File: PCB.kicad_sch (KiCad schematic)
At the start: 20 parts, among them SW1 SW_Push_Dual, SW10 SW_Push_Dual, SW11 SW_Push_Dual, SW12 SW_Push_Dual, SW13 SW_Push_Dual, SW2 SW_Push_Dual, SW5 SW_Push_Dual, SW6 SW_Push_Dual, SW7 SW_Push_Dual, SW8 SW_Push_Dual, SW9 SW_Push_Dual, U1 STM32L010F4Px, U2 74HC165, U3 74HC165, U4 74HC165

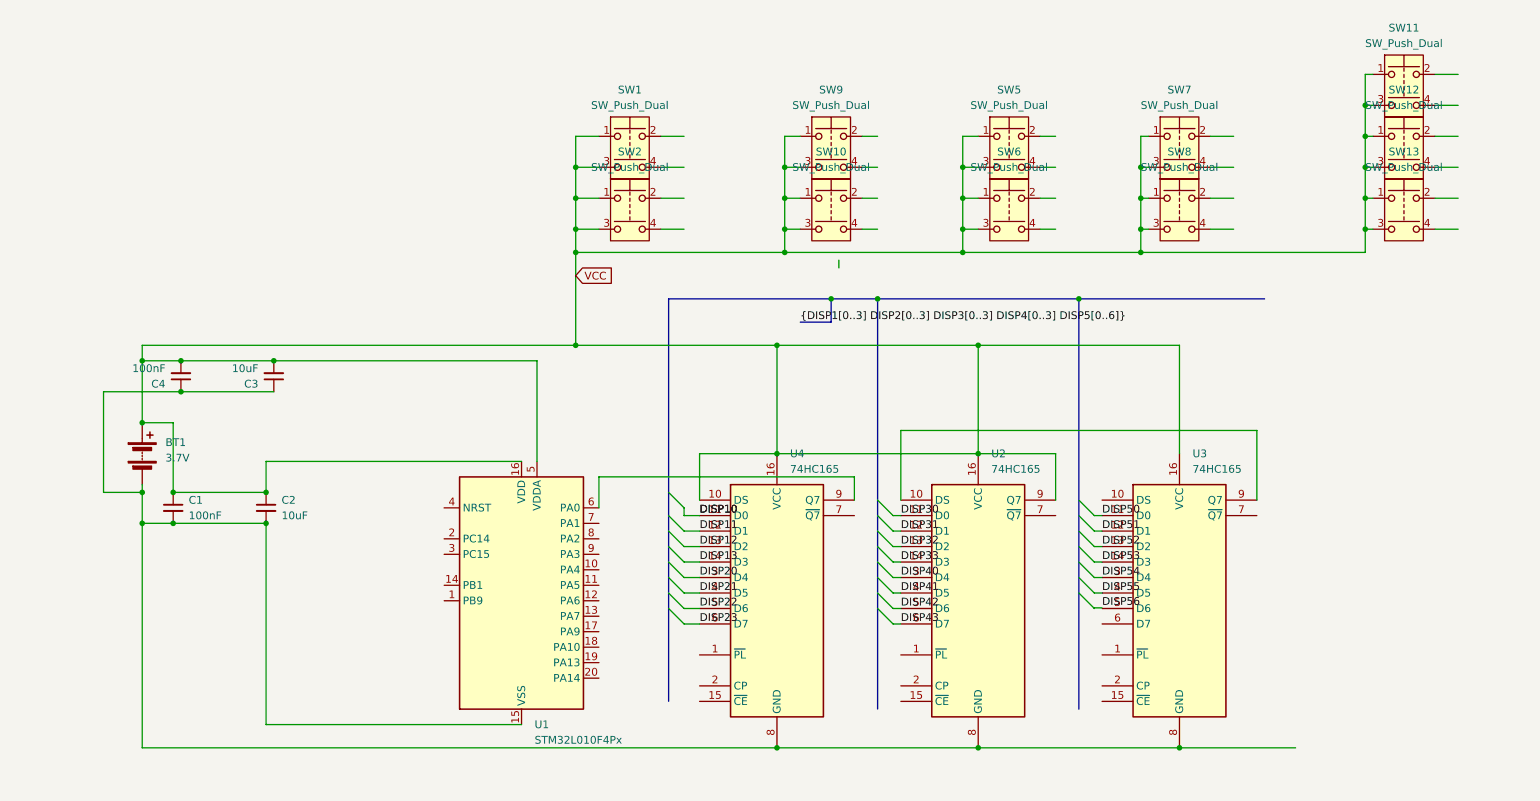
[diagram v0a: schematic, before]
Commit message: botones
añadidas las conexiones de los botones con pull down resistors
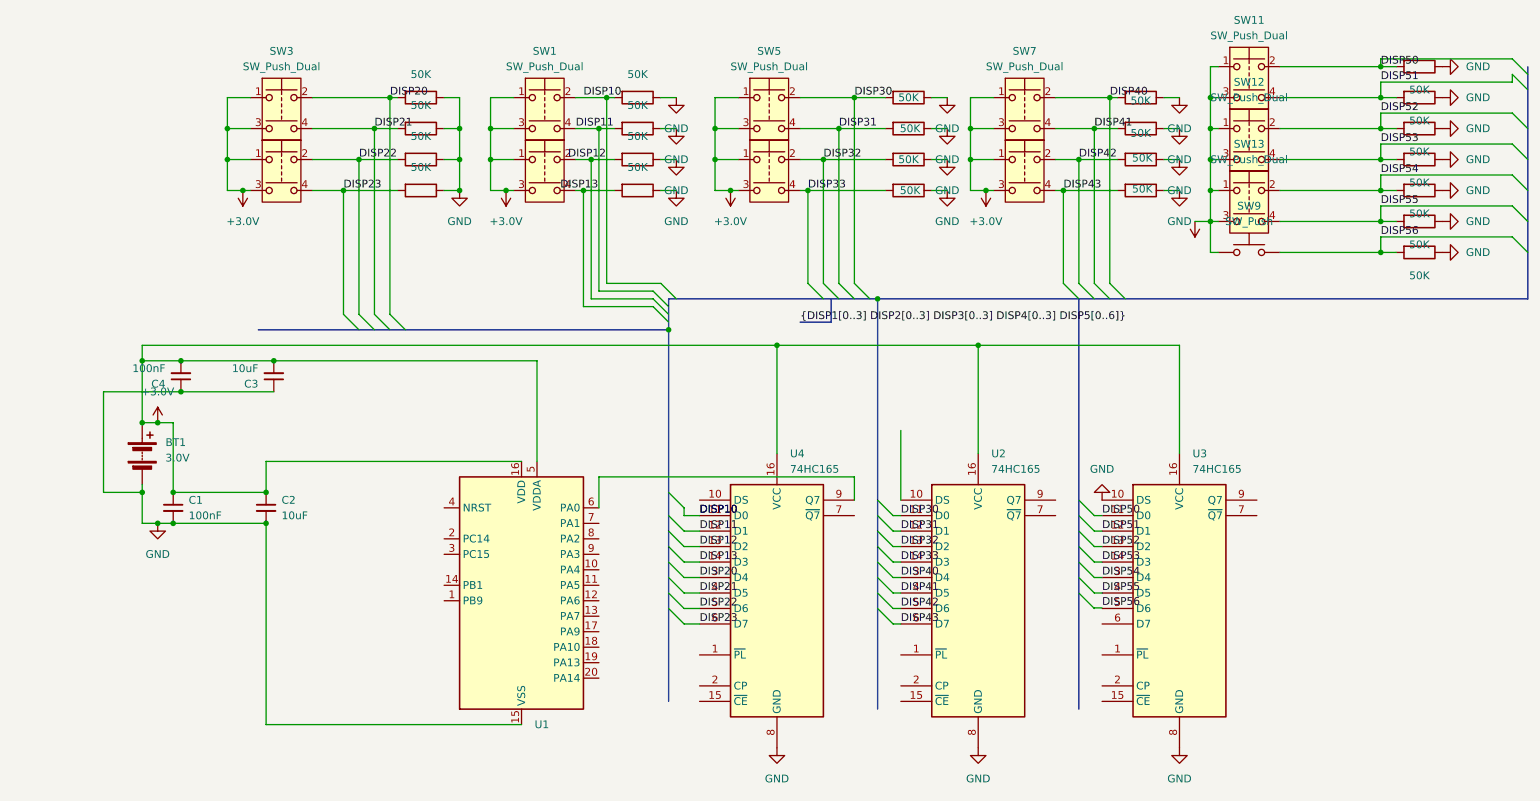
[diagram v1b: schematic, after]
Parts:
- removed SW10, SW9: SW_Push_Dual, symbol Switch:SW_Push_Dual
- added R, R1, R10, R11, R12, R13, R14, R15, R16, R2, R23, R24, R25, R26, R27, R28, R29, R3, R4, R5, R6, R7, R9: 50K, symbol Device:R
- added SW3, SW4: SW_Push_Dual, symbol Switch:SW_Push_Dual
- added SW9: SW_Push, symbol Switch:SW_Push
- BT1: value 3.7V -> 3.0V
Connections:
- net DISP10: now also SW1.2, R1.2
- net DISP11: now also SW1.4, R2.2
- net DISP20: now also R5.2, SW3.2
- net DISP21: now also R6.2, SW3.4
- net DISP22: now also R7.2, SW4.2
- net DISP23: now also R.2, SW4.4
- net DISP30: now also SW5.2, R9.2
- net DISP31: now also SW5.4, R10.2
- net DISP32: now also SW6.2, R11.2
- net DISP33: now also SW6.4, R12.2
- net DISP40: now also SW7.2, R13.2
- net DISP41: now also SW7.4, R14.2
- net DISP42: now also SW8.2, R15.2
- net DISP43: now also SW8.4, R16.2
- net DISP50: now also SW11.2, R29.2
- net DISP51: now also SW11.4, R28.2
- net DISP52: now also SW12.2, R27.2
- net DISP53: now also SW12.4, R26.2
- net DISP54: now also SW13.2, R25.2
- net DISP55: now also SW13.4, R24.2
- net DISP56: now also R23.2, SW9.2
- net GND: now reaches BT1.2 (-), C1.2, C2.2, C3.1, C4.1, U1.15 (VSS), U2.8 (GND), U3.8 (GND), U4.8 (GND)
- net GND: now also U3.10 (DS), R.1, R1.1, R10.1, R11.1, R12.1, R13.1, R14.1, R15.1, R16.1, R2.1, R23.1, R24.1, R25.1, R26.1, R27.1, R28.1, R29.1, R3.1, R4.1, R5.1, R6.1, R7.1, R9.1
- net at U2.10 (DS): no longer U3.9 (Q7)
- net at SW2.2: now also R3.2
- net at SW2.4: now also R4.2
- net VCC renamed +3.0V
- net +3.0V: now also SW3.1, SW3.3, SW4.1, SW4.3, SW9.1; no longer U2.9 (Q7), U4.10 (DS)
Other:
- moved on the sheet: SW1, SW11, SW12, SW13

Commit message: MCU y Resgistros
Creado el cableado para programar la MCU y para conectarla a los registros
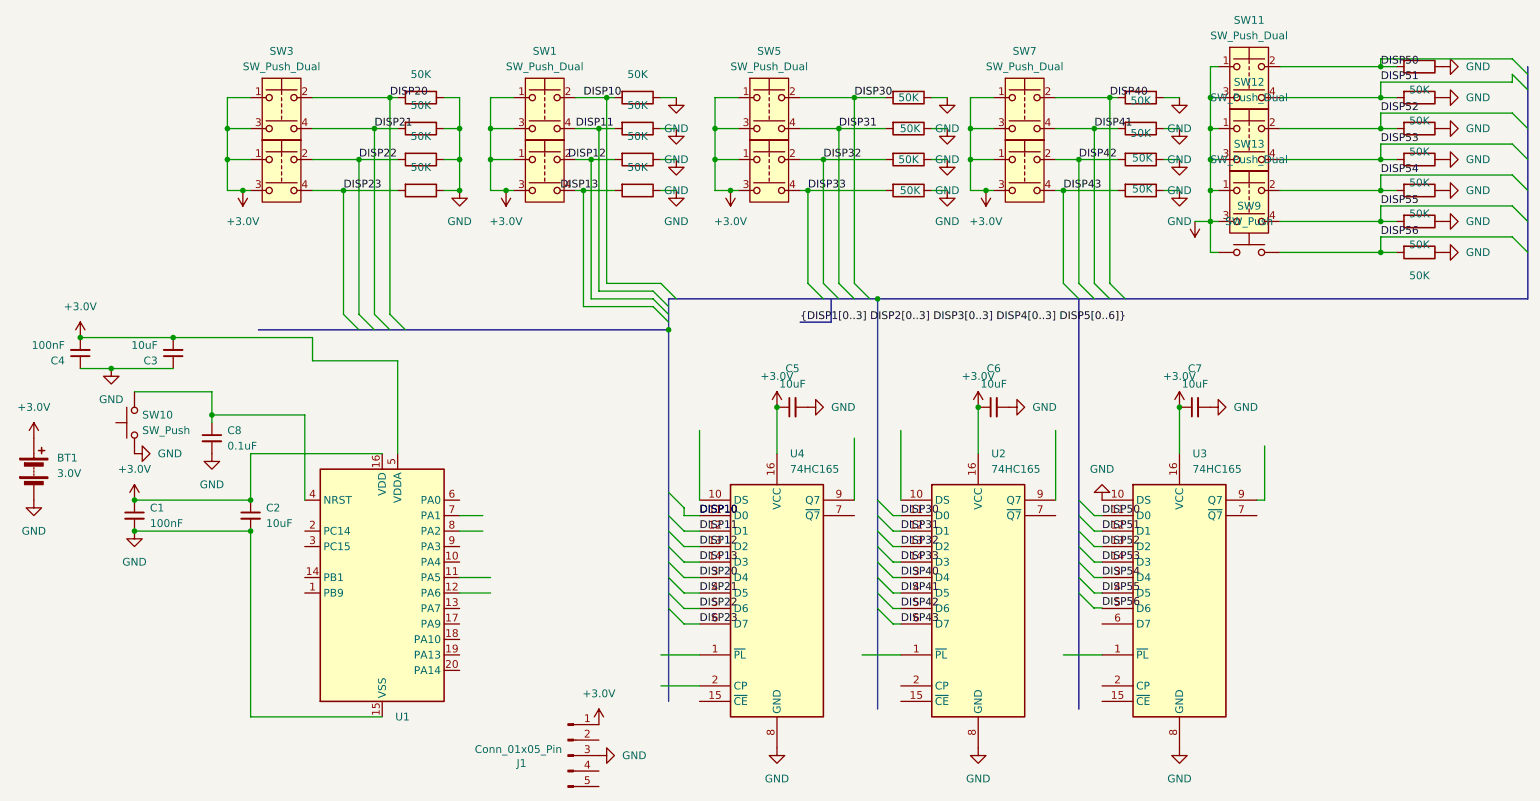
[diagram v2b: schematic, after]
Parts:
- added C5, C6, C7: 10uF, symbol Device:C_Small
- added C8: 0.1uF, symbol Device:C_Small
- added J1: Conn_01x05_Pin, symbol Connector:Conn_01x05_Pin
- added SW10: SW_Push, symbol Switch:SW_Push
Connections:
- net +3.0V: now also C5.1, C6.1, C7.1, J1.1 (Pin_1)
- net GND: now also C5.2, C6.2, C7.2, C8.2, J1.3 (Pin_3), SW10.1
- net at U2.1 (~{PL}): no longer names the net of U2.1 (~{PL})
- net at U2.1 (~{PL}): now also U1.11 (PA5), U1.12 (PA6), U1.19 (PA13), U1.20 (PA14), U1.4 (NRST), U1.7 (PA1), U1.8 (PA2), U2.10 (DS), U2.15 (~{CE}), U2.2 (CP), U2.9 (Q7), U3.1 (~{PL}), U3.15 (~{CE}), U3.2 (CP), U3.9 (Q7), U4.1 (~{PL}), U4.10 (DS), U4.15 (~{CE}), U4.2 (CP), U4.9 (Q7), C8.1, J1.2 (Pin_2), J1.4 (Pin_4), J1.5 (Pin_5), SW10.2
- net at U1.6 (PA0): no longer U4.9 (Q7)
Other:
- moved on the sheet: BT1, C1, C2, C3, C4, U1
